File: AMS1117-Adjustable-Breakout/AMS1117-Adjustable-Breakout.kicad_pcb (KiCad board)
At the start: 2 copper layers, 32.4 x 20.6 mm, 14 parts, among them J1 Input, J2 Output, U1 AMS1117

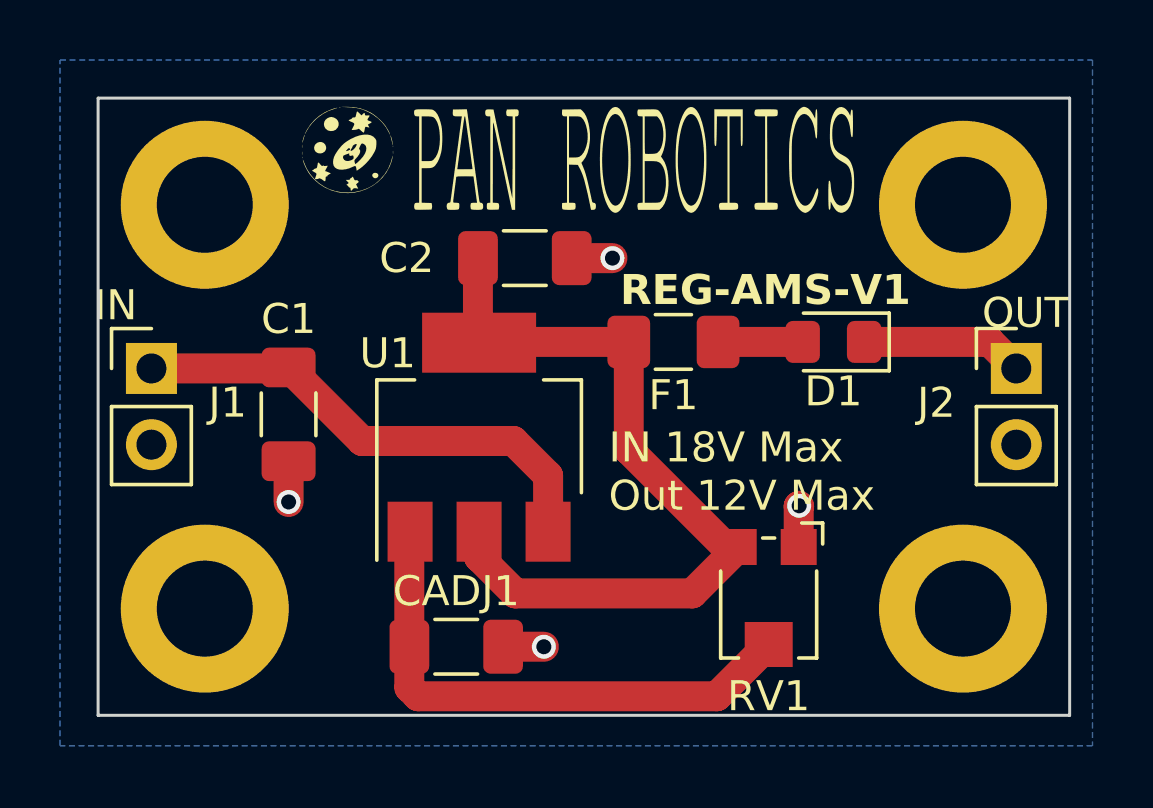
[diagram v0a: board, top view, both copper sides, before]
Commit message: Board Length Reduced
AD 03/09/23
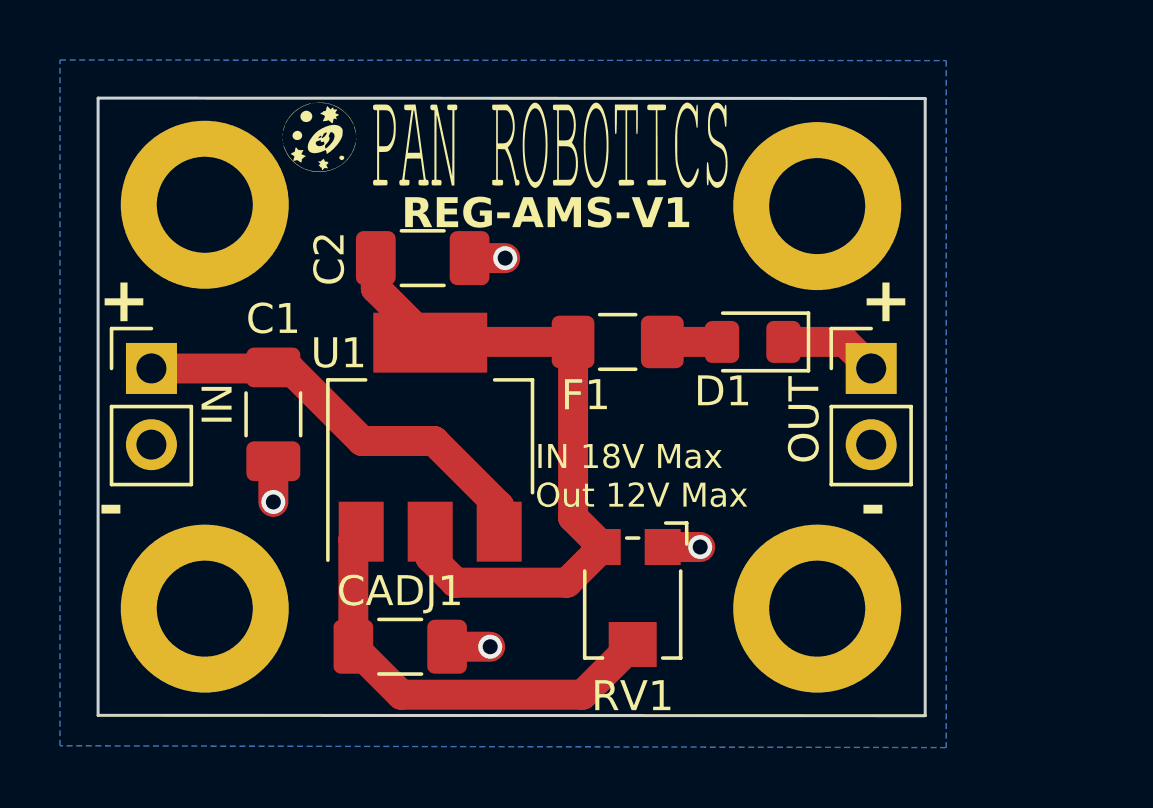
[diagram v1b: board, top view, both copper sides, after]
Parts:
- removed the G*** at (90.9, 46.5)
- added G***: LOGO, AMS1117-Adjustable-Breakout:Pan-Robotics-Logo6, F.Cu at (88.5, 46.0)
- moved H3 4.86 mm to (98.9, 48.0)
- moved H4 4.86 mm to (98.9, 61.5)
- moved J2 4.84 mm to (100.7, 53.5)
- moved RV1 4.53 mm to (92.8, 61.2)
- moved C2 3.40 mm to (85.8, 49.8)
- moved D1 2.69 mm to (96.8, 52.6)
- moved CADJ1 1.87 mm to (85.0, 62.7)
- moved F1 1.86 mm to (92.2, 52.6)
- moved U1 1.63 mm to (86.0, 55.8)
- moved C1 0.51 mm to (80.8, 55.0)
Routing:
- net Net-(U1-VO): track 27.1 -> 23.0 mm
- net Net-(U1-ADJ): track 18.0 -> 14.6 mm
- net Net-(J1-Pin_1): track 16.6 -> 14.4 mm
- net Net-(D1-K): track 5.44 -> 3.34 mm
- net Net-(D1-A): track 2.82 -> 1.99 mm
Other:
- board size 32.4 x 20.6 mm -> 27.6 x 20.6 mm
- board text added: "+"
- board text added: "-"
